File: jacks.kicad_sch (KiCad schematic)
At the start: 73 parts, among them J1 PJ366ST, J10 PJ398SM, J11 PJ398SM, J12 PJ398SM, J13 PJ398SM, J14 PJ398SM, J15 PJ398SM, J16 PJ398SM, J17 PJ398SM, J18 PJ398SM, J19 PJ398SM, J2 PJ366ST, J20 PJ398SM, J21 PJ398SM, J22 PJ398SM, J23 PJ398SM, J24 PJ398SM, J25 PJ398SM, J26 PJ398SM, J3 PJ398SM, J4 PJ398SM, J5 PJ398SM, J6 PJ398SM, J7 PJ398SM, J8 PJ398SM, J9 PJ398SM, Q1 MMBT3904, Q2 MMBT3904, Q3 MMBT3904, Q4 MMBT3904, U1 VO0600T, U2 74LV1T34, U6 MCP6004

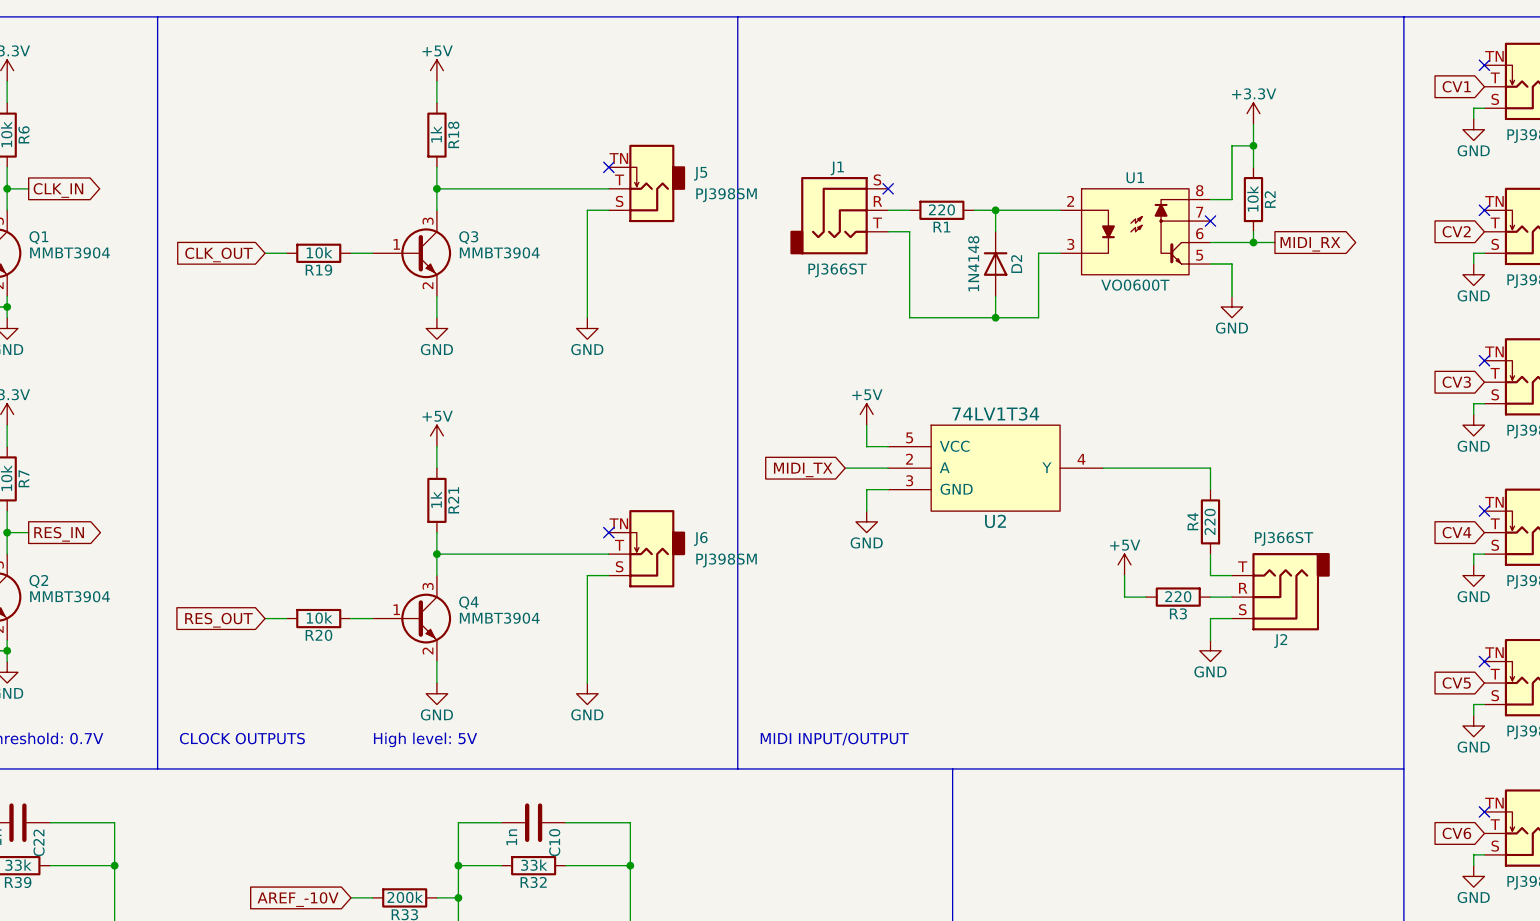
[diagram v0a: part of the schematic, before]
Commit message: Added switches for selecting the MIDI type
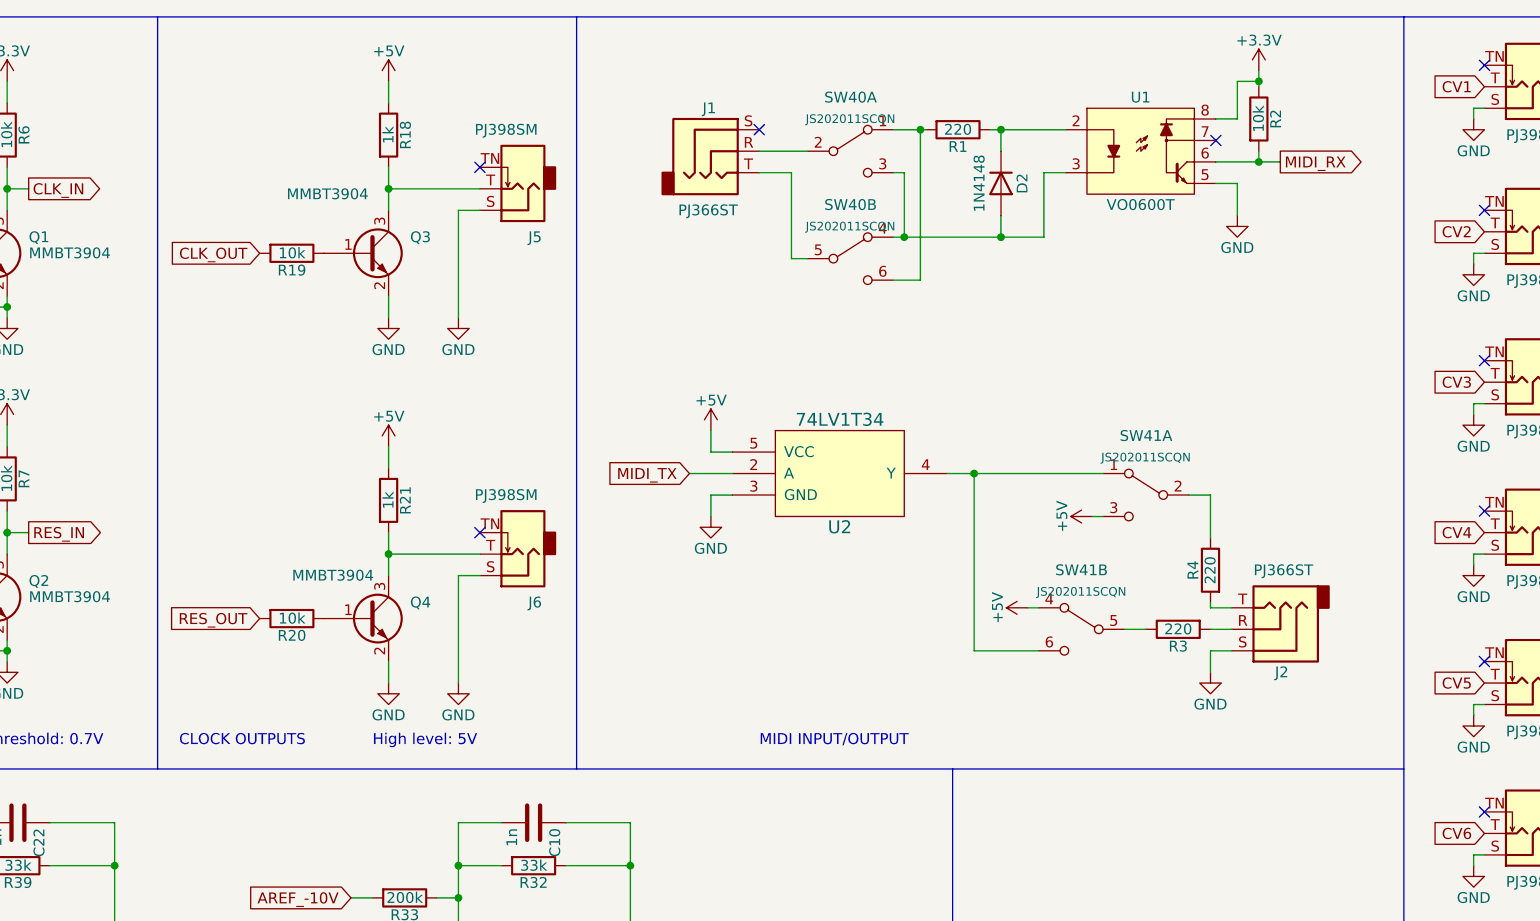
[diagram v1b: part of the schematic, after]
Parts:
- added SW40, SW41: JS202011SCQN, seq:SW_DPDT_CK_JS202011SCQN, symbol Switch:SW_DPDT_x2
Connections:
- net +5V: now also SW41.3 (C), SW41.4 (A); no longer R3.1
- net at D2.2 (A), U1.3: now also SW40.3 (C), SW40.4 (A); no longer J1.T
- net at R1.2: now also SW40.1 (A), SW40.6 (C); no longer J1.R
- net at R4.1: now also SW41.2 (B); no longer U2.4 (Y)
- new net: R3.1, SW41.5 (B)
- new net: SW41.1 (A), SW41.6 (C), U2.4 (Y)
- new net: J1.T, SW40.5 (B)
- new net: J1.R, SW40.2 (B)
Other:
- moved on the sheet: D2, J1, J2, J5, J6, Q3, Q4, R1, R18, R19, R2, R20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
